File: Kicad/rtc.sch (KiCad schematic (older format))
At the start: 6 parts, among them U901 MCP7940N, Y901 32,768 Hz

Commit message: Update component values.
Tolerance and Voltage are set to the minimum acceptable. The selected
parts can be better, where a better part is cheaper or has
better availability.

Also dropped R2R DAC tolerance to 1% - 0.5% was overkill. The output
resistor had the wrong value too, which is fixed.
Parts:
- C901, C902: Tolerance (none) -> C0G; Voltage C0G -> 50V
- C903: Tolerance (none) -> X5R; Voltage (none) -> 50V
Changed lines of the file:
@@
 F 8 "579-MCP7940N-I/P" H 4075 2675 50  0001 C CNN "Mouser"
 F 9 "C51106" H 4075 2675 50  0001 C CNN "LCSC Part#"
+F 10 "~" H 4075 2675 50  0001 C CNN "Tolerance"
+F 11 "~" H 4075 2675 50  0001 C CNN "Voltage"
 	1    4075 2675
 	1    0    0    -1
@@
 F 7 "36-103-ND" H 6300 3400 50  0001 C CNN "Digikey"
 F 8 "~" H 6300 3400 50  0001 C CNN "LCSC Part#"
+F 9 "~" H 6300 3400 50  0001 C CNN "Mouser"
+F 10 "~" H 6300 3400 50  0001 C CNN "Tolerance"
+F 11 "~" H 6300 3400 50  0001 C CNN "Voltage"
 	1    6300 3400
 	1    0    0    -1
@@
 F 4 "CPL" H 0   0   50  0001 C CNN "Manufacturer"
 F 5 "0" H 7050 3350 50  0001 C CNN "DNP"
-F 6 "" H 7050 3350 50  0001 C CNN "Digikey"
+F 6 "~" H 7050 3350 50  0001 C CNN "Digikey"
 F 7 "CPL-CAP-X7R-0805-100NF-50V" H 7050 3350 50  0001 C CNN "MPN"
-F 8 "" H 7050 3350 50  0001 C CNN "Mouser"
+F 8 "~" H 7050 3350 50  0001 C CNN "Mouser"
 F 9 "C49678" H 7050 3350 50  0001 C CNN "LCSC Part#"
+F 10 "X5R" H 7050 3350 50  0001 C CNN "Tolerance"
+F 11 "50V" H 7050 3350 50  0001 C CNN "Voltage"
 	1    7050 3350
 	1    0    0    -1
@@
 F 8 "CFS-20632768DZBB" H 5025 3000 50  0001 C CNN "Mouser"
 F 9 "~" H 5025 3000 50  0001 C CNN "LCSC Part#"
+F 10 "~" H 5025 3000 50  0001 C CNN "Tolerance"
+F 11 "~" H 5025 3000 50  0001 C CNN "Voltage"
 	1    5025 3000
 	-1   0    0    1
@@
 F 8 "603-CC805DRNPO9BN6R0" H 5350 3500 50  0001 C CNN "Mouser"
 F 9 "C67560" H 5350 3500 50  0001 C CNN "LCSC Part#"
-F 10 "C0G" H 5350 3500 50  0001 C CNN "Voltage"
+F 10 "50V" H 5350 3500 50  0001 C CNN "Voltage"
+F 11 "C0G" H 5350 3500 50  0001 C CNN "Tolerance"
 	1    5350 3500
 	1    0    0    -1
@@
 F 8 "603-CC805DRNPO9BN6R0" H 4700 3500 50  0001 C CNN "Mouser"
 F 9 "C67560" H 4700 3500 50  0001 C CNN "LCSC Part#"
-F 10 "C0G" H 4700 3500 50  0001 C CNN "Voltage"
+F 10 "50V" H 4700 3500 50  0001 C CNN "Voltage"
+F 11 "C0G" H 4700 3500 50  0001 C CNN "Tolerance"
 	1    4700 3500
 	1    0    0    -1

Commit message: Drop capacitor voltage ratings where possible.
Audio circuit is 1V RMS, so 6.3V is fine.
Use 10V for 3.3V circuits.
Use 16V for 5.0V circuits.
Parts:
- C901, C902, C903: Voltage 50V -> 10V
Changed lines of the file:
@@
 F 9 "C49678" H 7050 3350 50  0001 C CNN "LCSC Part#"
 F 10 "X5R" H 7050 3350 50  0001 C CNN "Tolerance"
-F 11 "50V" H 7050 3350 50  0001 C CNN "Voltage"
+F 11 "10V" H 7050 3350 50  0001 C CNN "Voltage"
 	1    7050 3350
 	1    0    0    -1
@@
 F 8 "603-CC805DRNPO9BN6R0" H 5350 3500 50  0001 C CNN "Mouser"
 F 9 "C67560" H 5350 3500 50  0001 C CNN "LCSC Part#"
-F 10 "50V" H 5350 3500 50  0001 C CNN "Voltage"
+F 10 "10V" H 5350 3500 50  0001 C CNN "Voltage"
 F 11 "C0G" H 5350 3500 50  0001 C CNN "Tolerance"
 	1    5350 3500
@@
 F 8 "603-CC805DRNPO9BN6R0" H 4700 3500 50  0001 C CNN "Mouser"
 F 9 "C67560" H 4700 3500 50  0001 C CNN "LCSC Part#"
-F 10 "50V" H 4700 3500 50  0001 C CNN "Voltage"
+F 10 "10V" H 4700 3500 50  0001 C CNN "Voltage"
 F 11 "C0G" H 4700 3500 50  0001 C CNN "Tolerance"
 	1    4700 3500

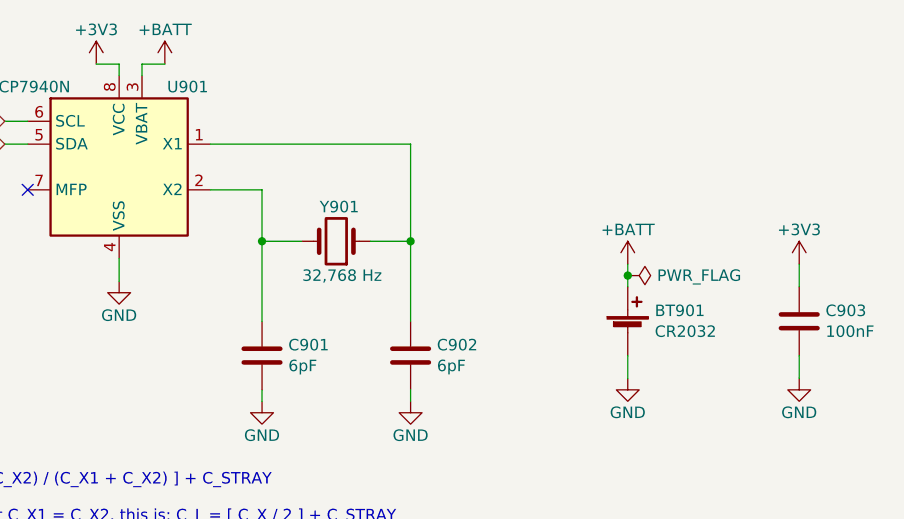
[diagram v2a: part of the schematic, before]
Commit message: Added expansion header.
Involved rerouting quite a few things.
Also added through-hole switches for power/reset.
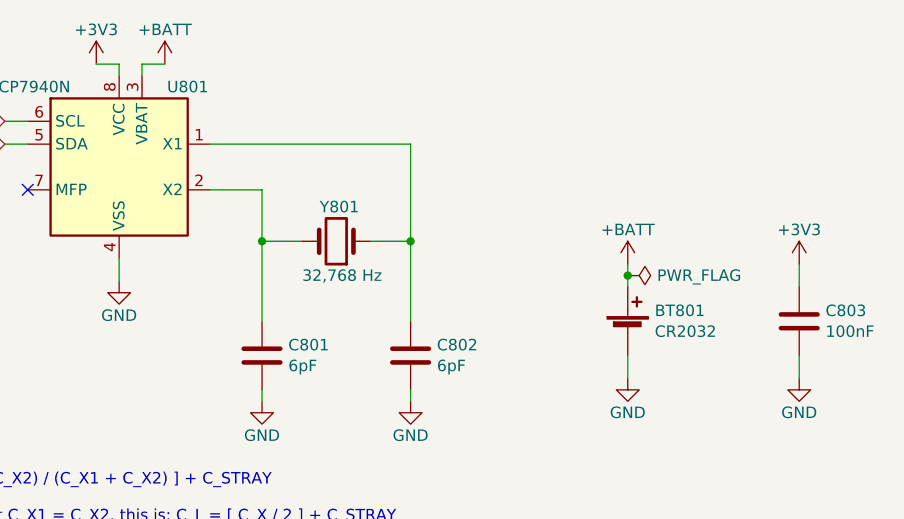
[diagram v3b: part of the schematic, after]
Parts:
- renumbered BT901 to BT801, C901 to C801, C902 to C802, C903 to C803, U901 to U801, Y901 to Y801
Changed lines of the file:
@@
 I2C_SCL
 $Comp
-L Timer:MCP7940N-xP U901
+L Timer:MCP7940N-xP U801
 U 1 1 5E0F47D7
 P 4075 2675
-F 0 "U901" H 4375 3025 50  0000 C CNN
+F 0 "U801" H 4375 3025 50  0000 C CNN
 F 1 "MCP7940N" H 3675 3025 50  0000 C CNN
 F 2 "Package_DIP:DIP-8_W7.62mm" H 4075 2675 50  0001 C CNN
@@
 $EndComp
 $Comp
-L Device:Battery_Cell BT901
+L Device:Battery_Cell BT801
 U 1 1 5E0F507E
 P 6300 3400
-F 0 "BT901" H 6418 3496 50  0000 L CNN
+F 0 "BT801" H 6418 3496 50  0000 L CNN
 F 1 "CR2032" H 6418 3405 50  0000 L CNN
 F 2 "Neotron-Common-Hardware:BatteryHolder_Keystone_103_1x20mm" V 6300 3460 50  0001 C CNN
@@
 AR Path="/5DF1D0B0/5E0203C5" Ref="#PWR?"  Part="1"
 AR Path="/5DF66898/5E0203C5" Ref="#PWR?"  Part="1"
-AR Path="/5FEF404D/5E0203C5" Ref="#PWR0908"  Part="1"
-F 0 "#PWR0908" H 7050 2950 50  0001 C CNN
+AR Path="/5FEF404D/5E0203C5" Ref="#PWR0808"  Part="1"
+F 0 "#PWR0808" H 7050 2950 50  0001 C CNN
 F 1 "+3V3" H 7050 3250 50  0000 C CNN
 F 2 "" H 7050 3100 50  0001 C CNN
@@
 AR Path="/5DF1D0B0/5E0203CB" Ref="C?"  Part="1"
 AR Path="/5DF66898/5E0203CB" Ref="C?"  Part="1"
-AR Path="/5FEF404D/5E0203CB" Ref="C903"  Part="1"
-F 0 "C903" H 7165 3396 50  0000 L CNN
+AR Path="/5FEF404D/5E0203CB" Ref="C803"  Part="1"
+F 0 "C803" H 7165 3396 50  0000 L CNN
 F 1 "100nF" H 7165 3305 50  0000 L CNN
 F 2 "Capacitor_SMD:C_0805_2012Metric_Pad1.18x1.45mm_HandSolder" H 7088 3200 50  0001 C CNN
@@
 AR Path="/5DF1D0B0/5E0203D1" Ref="#PWR?"  Part="1"
 AR Path="/5DF66898/5E0203D1" Ref="#PWR?"  Part="1"
-AR Path="/5FEF404D/5E0203D1" Ref="#PWR0909"  Part="1"
-F 0 "#PWR0909" H 7050 3350 50  0001 C CNN
+AR Path="/5FEF404D/5E0203D1" Ref="#PWR0809"  Part="1"
+F 0 "#PWR0809" H 7050 3350 50  0001 C CNN
 F 1 "GND" H 7050 3450 50  0000 C CNN
 F 2 "" H 7050 3600 50  0001 C CNN
@@
 NoConn ~ 3675 2775
 $Comp
-L power:+3V3 #PWR0901
+L power:+3V3 #PWR0801
 U 1 1 5E027CB5
 P 3975 2225
-F 0 "#PWR0901" H 3975 2075 50  0001 C CNN
+F 0 "#PWR0801" H 3975 2075 50  0001 C CNN
 F 1 "+3V3" H 3975 2375 50  0000 C CNN
 F 2 "" H 3975 2225 50  0001 C CNN
@@
 AR Path="/5DF1D0B0/5E02823D" Ref="#PWR?"  Part="1"
 AR Path="/5DF66898/5E02823D" Ref="#PWR?"  Part="1"
-AR Path="/5FEF404D/5E02823D" Ref="#PWR0902"  Part="1"
-F 0 "#PWR0902" H 4075 2925 50  0001 C CNN
+AR Path="/5FEF404D/5E02823D" Ref="#PWR0802"  Part="1"
+F 0 "#PWR0802" H 4075 2925 50  0001 C CNN
 F 1 "GND" H 4075 3025 50  0000 C CNN
 F 2 "" H 4075 3175 50  0001 C CNN
@@
 $EndComp
 $Comp
-L Device:Crystal Y901
+L Device:Crystal Y801
 U 1 1 5E028A76
 P 5025 3000
-F 0 "Y901" H 4925 2850 50  0000 L CNN
+F 0 "Y801" H 4925 2850 50  0000 L CNN
 F 1 "32,768 Hz" H 4825 3150 50  0000 L CNN
 F 2 "Crystal:Crystal_DS26_D2.0mm_L6.0mm_Horizontal" H 5025 3000 50  0001 C CNN
@@
 	4075 3075 4075 3175
 $Comp
-L power:+BATT #PWR0903
+L power:+BATT #PWR0803
 U 1 1 5E0292FA
 P 4275 2225
-F 0 "#PWR0903" H 4275 2075 50  0001 C CNN
+F 0 "#PWR0803" H 4275 2075 50  0001 C CNN
 F 1 "+BATT" H 4275 2375 50  0000 C CNN
 F 2 "" H 4275 2225 50  0001 C CNN
@@
 	4175 2225 4275 2225
 $Comp
-L power:+BATT #PWR0906
+L power:+BATT #PWR0806
 U 1 1 5E029FFB
 P 6300 3100
-F 0 "#PWR0906" H 6300 2950 50  0001 C CNN
+F 0 "#PWR0806" H 6300 2950 50  0001 C CNN
 F 1 "+BATT" H 6300 3250 50  0000 C CNN
 F 2 "" H 6300 3100 50  0001 C CNN
@@
 AR Path="/5DF1D0B0/5E02A51C" Ref="#PWR?"  Part="1"
 AR Path="/5DF66898/5E02A51C" Ref="#PWR?"  Part="1"
-AR Path="/5FEF404D/5E02A51C" Ref="#PWR0907"  Part="1"
-F 0 "#PWR0907" H 6300 3350 50  0001 C CNN
+AR Path="/5FEF404D/5E02A51C" Ref="#PWR0807"  Part="1"
+F 0 "#PWR0807" H 6300 3350 50  0001 C CNN
 F 1 "GND" H 6300 3450 50  0000 C CNN
 F 2 "" H 6300 3600 50  0001 C CNN
@@
 	6300 3500 6300 3600
 $Comp
-L Device:C C902
+L Device:C C802
 U 1 1 5E02C5CE
 P 5350 3500
-F 0 "C902" H 5465 3546 50  0000 L CNN
+F 0 "C802" H 5465 3546 50  0000 L CNN
 F 1 "6pF" H 5465 3455 50  0000 L CNN
 F 2 "Capacitor_SMD:C_0805_2012Metric_Pad1.18x1.45mm_HandSolder" H 5388 3350 50  0001 C CNN
@@
 $EndComp
 $Comp
-L Device:C C901
+L Device:C C801
 U 1 1 5E02CC31
 P 4700 3500
-F 0 "C901" H 4815 3546 50  0000 L CNN
+F 0 "C801" H 4815 3546 50  0000 L CNN
 F 1 "6pF" H 4815 3455 50  0000 L CNN
 F 2 "Capacitor_SMD:C_0805_2012Metric_Pad1.18x1.45mm_HandSolder" H 4738 3350 50  0001 C CNN
@@
 AR Path="/5DF1D0B0/5E02D069" Ref="#PWR?"  Part="1"
 AR Path="/5DF66898/5E02D069" Ref="#PWR?"  Part="1"
-AR Path="/5FEF404D/5E02D069" Ref="#PWR0904"  Part="1"
-F 0 "#PWR0904" H 4700 3450 50  0001 C CNN
+AR Path="/5FEF404D/5E02D069" Ref="#PWR0804"  Part="1"
+F 0 "#PWR0804" H 4700 3450 50  0001 C CNN
 F 1 "GND" H 4700 3550 50  0000 C CNN
 F 2 "" H 4700 3700 50  0001 C CNN
@@
 	4700 3650 4700 3700
 $Comp
-L power:PWR_FLAG #FLG0901
+L power:PWR_FLAG #FLG0801
 U 1 1 5E3BA2C7
 P 6300 3150
-F 0 "#FLG0901" H 6300 3225 50  0001 C CNN
+F 0 "#FLG0801" H 6300 3225 50  0001 C CNN
 F 1 "PWR_FLAG" V 6300 3278 50  0000 L CNN
 F 2 "" H 6300 3150 50  0001 C CNN
@@
 AR Path="/5DF1D0B0/5FF0B56D" Ref="#PWR?"  Part="1"
 AR Path="/5DF66898/5FF0B56D" Ref="#PWR?"  Part="1"
-AR Path="/5FEF404D/5FF0B56D" Ref="#PWR0905"  Part="1"
-F 0 "#PWR0905" H 5350 3450 50  0001 C CNN
+AR Path="/5FEF404D/5FF0B56D" Ref="#PWR0805"  Part="1"
+F 0 "#PWR0805" H 5350 3450 50  0001 C CNN
 F 1 "GND" H 5350 3550 50  0000 C CNN
 F 2 "" H 5350 3700 50  0001 C CNN
